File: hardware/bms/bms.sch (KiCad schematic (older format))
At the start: 199 parts, among them J1 Conn_01x08, J10 Conn_01x02, J11 Conn_01x02, J12 Conn_01x02, J13 Conn_01x10, J14 Conn_01x02, J15 Conn_01x02, J16 Cell Bypass, J2 Conn_01x04, J3 USB_B_Micro, J4 Conn_01x05, J5 Conn_01x04, J6 Conn_01x04, J7 Conn_01x03, J8 Conn_01x03, J9 Conn_01x02, M1 MountingHole, M2 MountingHole, M3 MountingHole, M4 MountingHole, M5 MountingHole, M6 MountingHole, Q1 BC817, Q10 ZXMP4A16G, Q11 IRF540N, Q12 IRF540N, Q13 BSS138, Q14 IRF540N, Q15 BSS138, Q16 BSS138, Q2 ZXMP4A16G, Q3 BSS138, Q4 BS170, Q5 IRF9540N, Q6 BC847, Q7 IRF9540N, Q8 BSS138, Q9 ZXMP4A16G, SW1 SW_DIP_x03, U1 USBLC6-2SC6, U2 STM32F042C6Tx, U3 TPS560430x3F, U4 TCAN334, U5 MAX485E, U6 LM5164DDAR, U7 LSI94202, Y1 8MHz

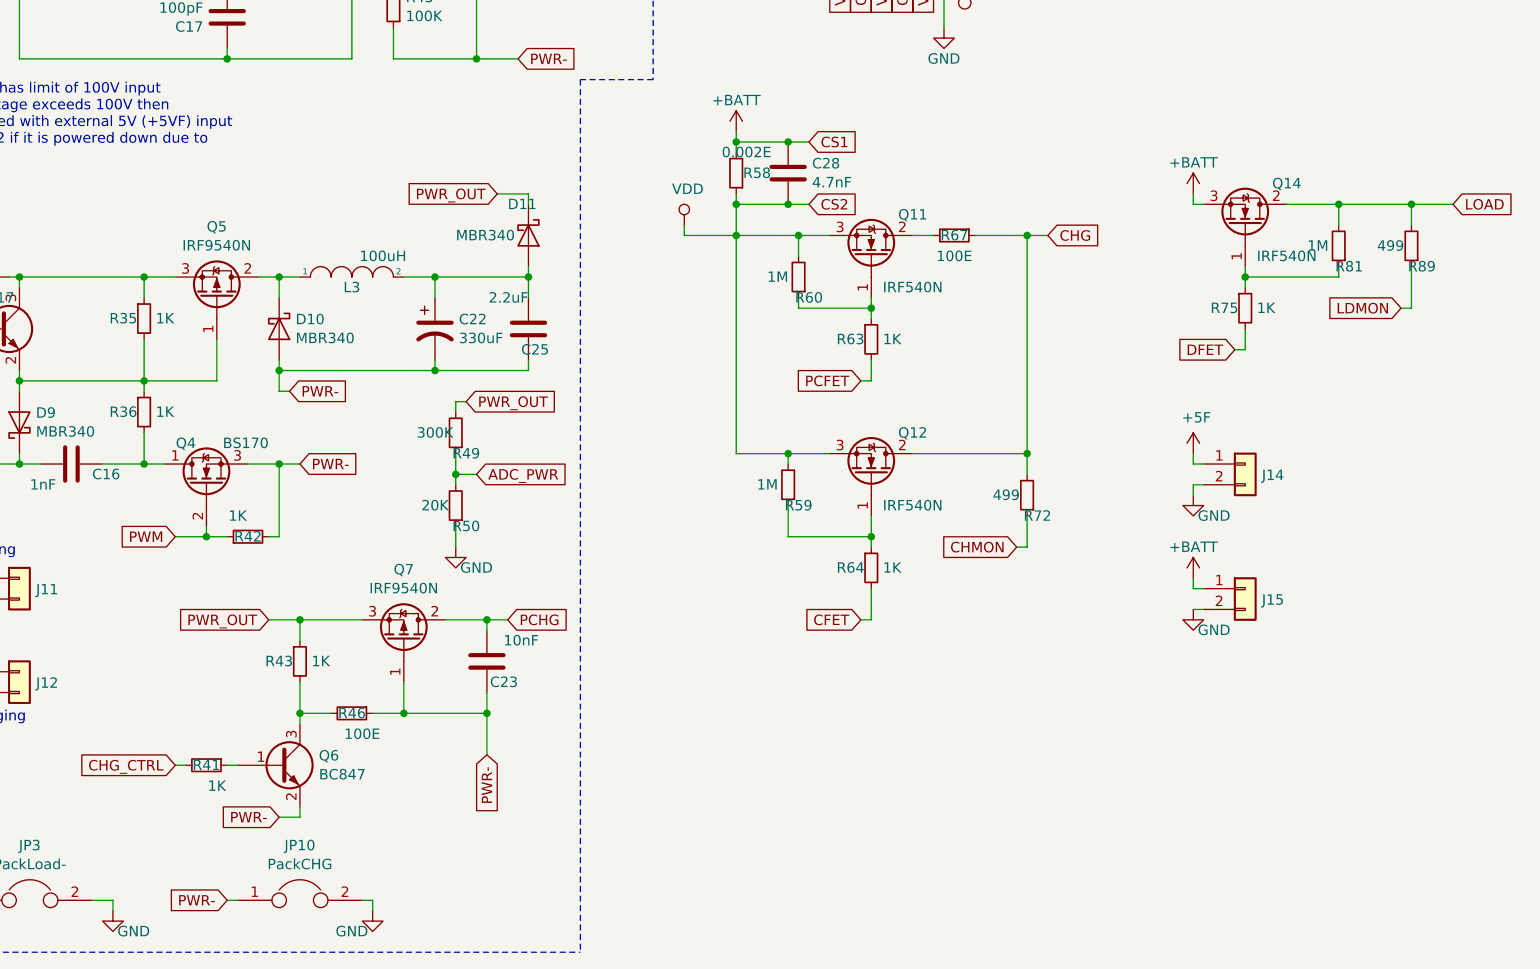
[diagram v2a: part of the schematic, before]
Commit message: fixed schematic errors, added isl94202 ref manual
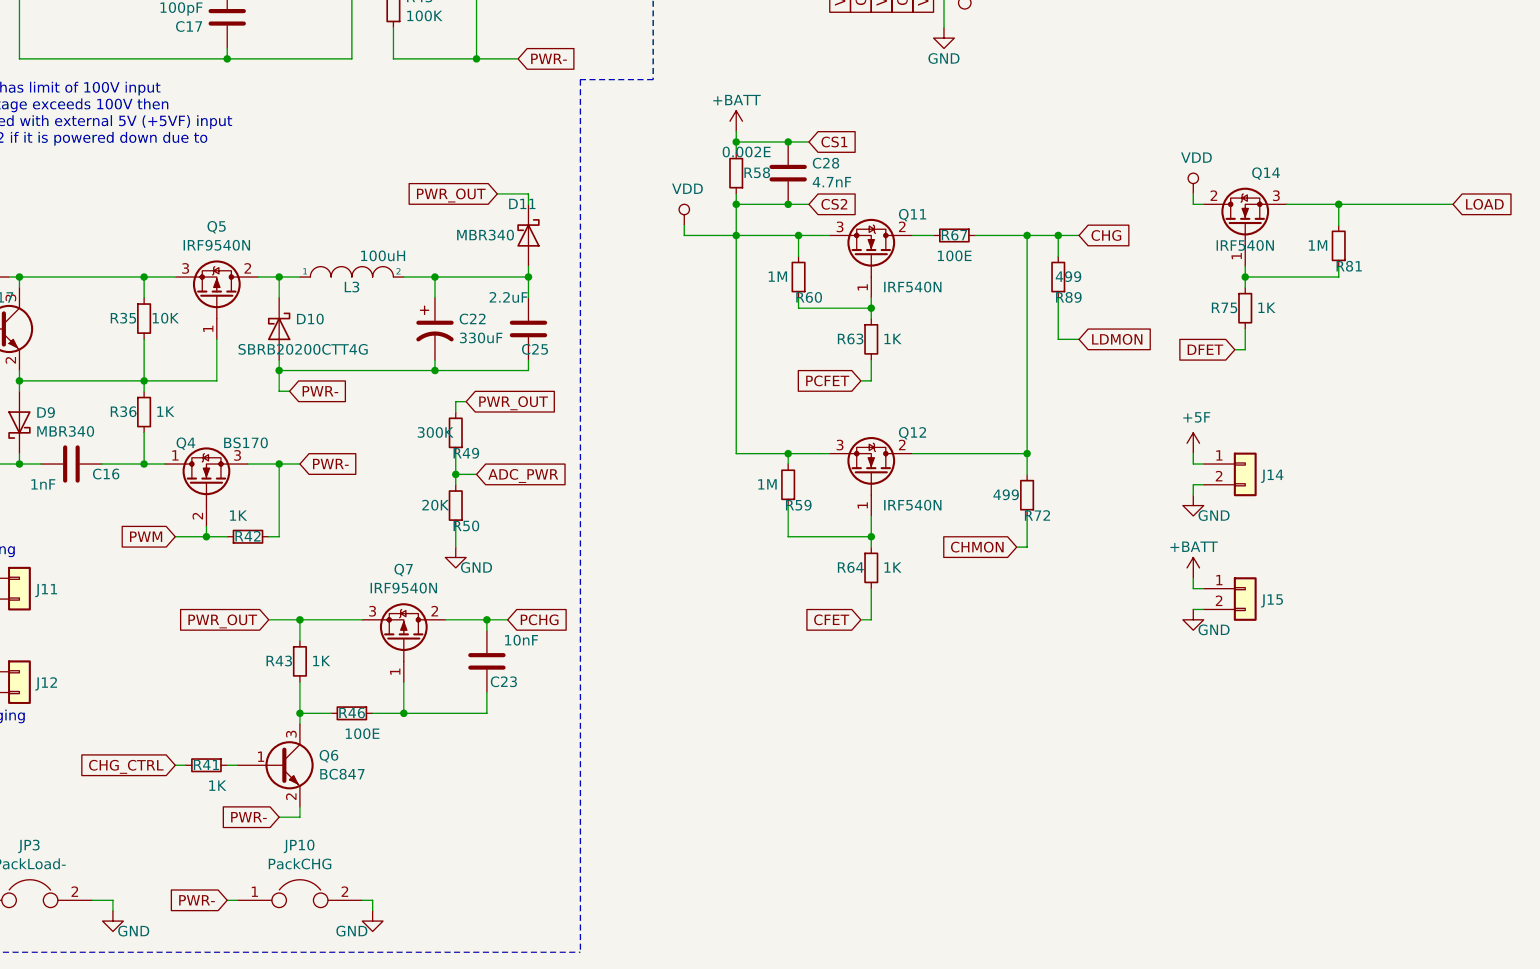
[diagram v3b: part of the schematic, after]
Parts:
- D10: value MBR340 -> SBRB20200CTT4G; footprint Diode_THT:D_DO-201AD_P15.24mm_Horizontal -> bms:D2PAK
- R35: value 1K -> 10K
- U1: footprint Package_SO:TSOP-6_1.65x3.05mm_P0.95mm -> Package_TO_SOT_SMD:SuperSOT-6
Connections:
- net +BATT: no longer Q14.3 (S)
- net CHG: now also R89.2
- net LOAD: now also Q14.3 (S); no longer Q14.2 (D), R89.2
- net PWR-: no longer C23.1, Q7.1 (G), R46.1
- net VDD: now also Q14.2 (D)
- new net: C23.1, Q7.1 (G), R46.1
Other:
- moved on the sheet: R89
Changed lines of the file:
@@
 F 0 "U1" H 1700 10766 50  0000 C CNN
 F 1 "USBLC6-2SC6" H 1700 10675 50  0000 C CNN
-F 2 "Package_SO:TSOP-6_1.65x3.05mm_P0.95mm" H 1700 9850 50  0001 C CNN
+F 2 "Package_TO_SOT_SMD:SuperSOT-6" H 1700 9850 50  0001 C CNN
 F 3 "" H 1450 10650 50  0001 C CNN
 	1    1700 10300
@@
 	1    0    0    -1
 $EndComp
-Text GLabel 13750 7600 2    50   Input ~ 0
+Text GLabel 13900 7600 2    50   Input ~ 0
 CHG
-Wire Wire Line
-	13400 7600 13650 7600
 Text GLabel 12850 8300 0    50   Input ~ 0
 PCFET
@@
 Connection ~ 13650 7600
 Wire Wire Line
-	13650 7600 13750 7600
+	13650 7600 13800 7600
 Wire Wire Line
 	12500 8700 12500 8650
@@
 Text GLabel 12850 9450 0    50   Input ~ 0
 CFET
-$Comp
-L power:+BATT #PWR0138
-U 1 1 5F6BE9DF
-P 14450 7400
-F 0 "#PWR0138" H 14450 7250 50  0001 C CNN
-F 1 "+BATT" H 14450 7550 50  0000 C CNN
-F 2 "" H 14450 7400 50  0001 C CNN
-F 3 "" H 14450 7400 50  0001 C CNN
-	1    14450 7400
-	1    0    0    -1
-$EndComp
 Wire Wire Line
 	14450 7400 14450 7450
@@
 Text GLabel 15700 7450 2    50   Input ~ 0
 LOAD
-Wire Wire Line
-	15150 7450 15500 7450
 Connection ~ 15150 7450
 $Comp
 L Device:R_Small R89
 U 1 1 5F80EB43
-P 15500 7650
-F 0 "R89" H 15450 7750 50  0000 C CNN
-F 1 "499" H 15600 7650 50  0000 C CNN
-F 2 "Resistor_SMD:R_0603_1608Metric_Pad1.05x0.95mm_HandSolder" H 15500 7650 50  0001 C CNN
-F 3 "~" H 15500 7650 50  0001 C CNN
-	1    15500 7650
+P 13800 7800
+F 0 "R89" H 13750 7900 50  0000 C CNN
+F 1 "499" H 13750 7800 50  0000 C CNN
+F 2 "Resistor_SMD:R_0603_1608Metric_Pad1.05x0.95mm_HandSolder" H 13800 7800 50  0001 C CNN
+F 3 "~" H 13800 7800 50  0001 C CNN
+	1    13800 7800
 	-1   0    0    1
 $EndComp
 Wire Wire Line
-	15500 7550 15500 7450
-Connection ~ 15500 7450
-Wire Wire Line
-	15500 7450 15700 7450
+	13800 7700 13800 7600
 $Comp
 L Device:R_Small R72
@@
 Text GLabel 13600 9100 0    50   Input ~ 0
 CHMON
-Text GLabel 15450 7950 0    50   Input ~ 0
+Text GLabel 13900 8100 2    50   Input ~ 0
 LDMON
 Wire Wire Line
@@
 	14700 8050 14700 8150
 Wire Wire Line
-	15450 7950 15500 7950
-Wire Wire Line
-	15500 7750 15500 7950
+	13800 7900 13800 8100
 $Comp
 L power:VDD #PWR0139
@@
 P 10050 8050
 F 0 "D10" V 10004 8129 50  0000 L CNN
-F 1 "MBR340" V 10095 8129 50  0000 L CNN
-F 2 "Diode_THT:D_DO-201AD_P15.24mm_Horizontal" H 10050 7875 50  0001 C CNN
+F 1 "SBRB20200CTT4G" V 10150 7850 50  0000 L CNN
+F 2 "bms:D2PAK" H 10050 7875 50  0001 C CNN
 F 3 "http://www.onsemi.com/pub_link/Collateral/MBR340-D.PDF" H 10050 8050 50  0001 C CNN
 	1    10050 8050
@@
 P 9400 8000
 F 0 "R35" H 9300 8000 50  0000 C CNN
-F 1 "1K" H 9500 8000 50  0000 C CNN
+F 1 "10K" H 9500 8000 50  0000 C CNN
 F 2 "Resistor_SMD:R_0603_1608Metric_Pad1.05x0.95mm_HandSolder" H 9400 8000 50  0001 C CNN
 F 3 "~" H 9400 8000 50  0001 C CNN
@@
 Wire Wire Line
 	10050 10400 10150 10400
-Text GLabel 11050 10100 3    50   Input ~ 0
-PWR-
-Wire Wire Line
-	11050 9900 11050 10100
-Connection ~ 11050 9900
 Text GLabel 9800 10800 0    50   Input ~ 0
 PWR-
@@
 	6950 9400 7050 9400
 $Comp
-L Transistor_FET:IRF540N Q11
-U 1 1 60664D6A
-P 12900 7700
-F 0 "Q11" V 13100 7900 50  0000 C CNN
-F 1 "IRF540N" V 12750 7900 50  0000 C CNN
-F 2 "Package_TO_SOT_SMD:TO-263-2" H 13150 7625 50  0001 L CIN
-F 3 "http://www.irf.com/product-info/datasheets/data/irf540n.pdf" H 12900 7700 50  0001 L CNN
-	1    12900 7700
-	0    1    -1   0
-$EndComp
-$Comp
 L Transistor_FET:IRF540N Q12
 U 1 1 606EC197
@@
 U 1 1 606EDC47
 P 14700 7550
-F 0 "Q14" V 14900 7750 50  0000 C CNN
-F 1 "IRF540N" V 14550 7750 50  0000 C CNN
+F 0 "Q14" V 14950 7450 50  0000 C CNN
+F 1 "IRF540N" V 14600 7550 50  0000 C CNN
 F 2 "Package_TO_SOT_SMD:TO-263-2" H 14950 7475 50  0001 L CIN
 F 3 "http://www.irf.com/product-info/datasheets/data/irf540n.pdf" H 14700 7550 50  0001 L CNN
 	1    14700 7550
-	0    1    -1   0
+	0    -1   -1   0
 $EndComp
 $Comp
@@
 Wire Notes Line
 	11500 6850 11500 11050
+$Comp
+L Transistor_FET:IRF540N Q11
+U 1 1 60664D6A
+P 12900 7700
+F 0 "Q11" V 13100 7900 50  0000 C CNN
+F 1 "IRF540N" V 12750 7900 50  0000 C CNN
+F 2 "Package_TO_SOT_SMD:TO-263-2" H 13150 7625 50  0001 L CIN
+F 3 "http://www.irf.com/product-info/datasheets/data/irf540n.pdf" H 12900 7700 50  0001 L CNN
+	1    12900 7700
+	0    1    -1   0
+$EndComp
+$Comp
+L power:VDD #PWR?
+U 1 1 60A78516
+P 14450 7400
+F 0 "#PWR?" H 14450 7250 50  0001 C CNN
+F 1 "VDD" H 14467 7573 50  0000 C CNN
+F 2 "" H 14450 7400 50  0001 C CNN
+F 3 "" H 14450 7400 50  0001 C CNN
+	1    14450 7400
+	1    0    0    -1
+$EndComp
+Wire Wire Line
+	15150 7450 15700 7450
+Connection ~ 13800 7600
+Wire Wire Line
+	13800 7600 13900 7600
+Wire Wire Line
+	13400 7600 13650 7600
+Wire Wire Line
+	13800 8100 13900 8100
 $EndSCHEMATC

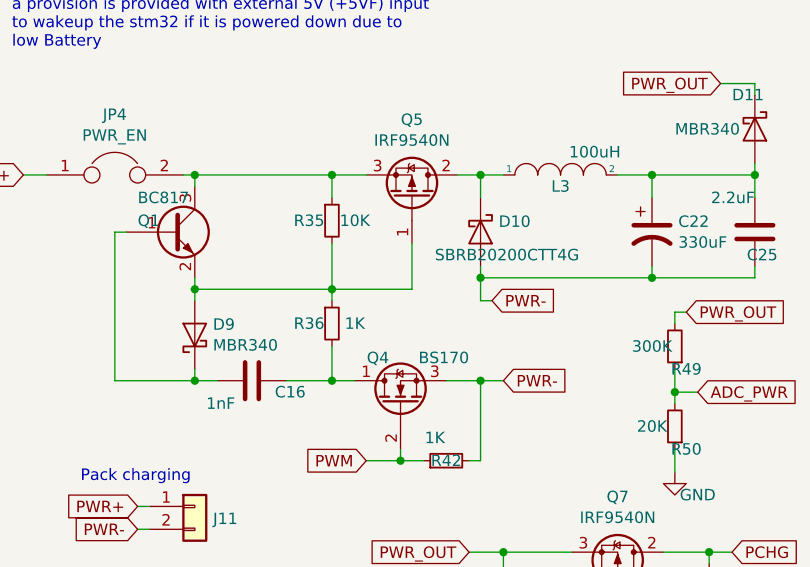
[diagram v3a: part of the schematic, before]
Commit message: footprint corrections
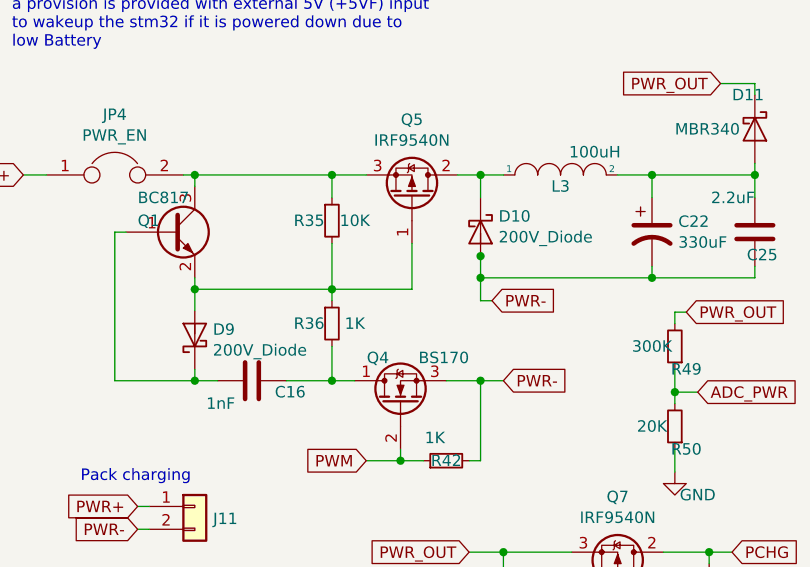
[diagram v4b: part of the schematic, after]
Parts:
- removed D10: SBRB20200CTT4G, bms:D2PAK, symbol Diode:MBR340
- removed D9: MBR340, Diode_THT:D_DO-201AD_P15.24mm_Horizontal, symbol Diode:MBR340
- added D10, D9: 200V_Diode, bms:D2PAK, symbol BMS:200V_Diode
- R2, R3, R33, R34, R37, R38, R39, R40, R51, R52, R54, R55, R56, R57, R65, R66, R68, R69, R70, R71, R78, R80, R83, R84, R85, R86, R87: footprint Resistor_SMD:R_1210_3225Metric_Pad1.42x2.65mm_HandSolder -> Resistor_SMD:R_0603_1608Metric_Pad1.05x0.95mm_HandSolder
- U4: footprint Package_SO:SOIC-8-N7_3.9x4.9mm_P1.27mm -> Package_SO:SOIC-8_3.9x4.9mm_P1.27mm
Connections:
- net PWR-: now also D10.1, D10.3
- net at Q1.2 (E), Q5.1 (G), R35.2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: now also D9.1, D9.3
- net at L3.1, Q5.2 (D): now also D10.4
- net at C16.2, Q1.1 (B): now also D9.4

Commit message: Added i2c level shifter
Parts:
- removed C25: 2.2uF, Capacitor_SMD:C_0603_1608Metric_Pad1.05x0.95mm_HandSolder, symbol Device:C
- removed D11: MBR340, Diode_THT:D_DO-201AD_P15.24mm_Horizontal, symbol Diode:MBR340
- added C25: 10uF, Capacitor_Tantalum_SMD:CP_EIA-7132-28_AVX-C, symbol Device:CP1
- added D11: 200V_Diode, bms:D2PAK, symbol BMS:200V_Diode
- added R90, R91: 4K7, Resistor_SMD:R_0603_1608Metric_Pad1.05x0.95mm_HandSolder, symbol Device:R_Small
- added R92: 200K, Resistor_SMD:R_0603_1608Metric_Pad1.05x0.95mm_HandSolder, symbol Device:R_Small
- added U8: PCA9306, Package_SO:SSOP-8_2.95x2.8mm_P0.65mm, symbol Interface:PCA9306
- C22: value 330uF -> 10uF; footprint Capacitor_Tantalum_SMD:CP_EIA-3528-21_Kemet-B -> Capacitor_Tantalum_SMD:CP_EIA-7132-28_AVX-C
- C23: value 10nF -> 0.01uF; footprint Capacitor_SMD:C_0603_1608Metric_Pad1.05x0.95mm_HandSolder -> Capacitor_SMD:C_1206_3216Metric_Pad1.42x1.75mm_HandSolder
- R49, R50: footprint Resistor_SMD:R_0603_1608Metric_Pad1.05x0.95mm_HandSolder -> Resistor_SMD:R_1206_3216Metric_Pad1.42x1.75mm_HandSolder
- R6, R9: value 2K2 -> 4K7
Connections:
- net CHG: no longer R89.2
- net GND: now also U7.49 (EP), U8.1 (GND)
- net LOAD: now also R89.2
- net PWR-: now also C25.2
- net PWR_OUT: now also D11.4
- net SCL: now also R91.1, U8.3 (SCL1); no longer R9.1, U2.42 (PB6)
- net SDA: now also R90.1, U8.4 (SDA1); no longer R6.1, U2.43 (PB7)
- net VCC: now also R92.1
- net RGO: now reaches TP5.1, U7.36 (RGO)
- net RGO: now also R90.2, R91.2, U8.2 (VREF1)
- net at C22.1, L3.2: now also C25.1, D11.1, D11.3
- new net: R92.2, U8.7 (VREF2), U8.8 (EN)
- new net SCL_3.3: R9.1, U2.42 (PB6), U8.6 (SCL2)
- new net SDA_3.3: R6.1, U2.43 (PB7), U8.5 (SDA2)
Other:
- moved on the sheet: D10, R6, R89, R9, TP5

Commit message: Schematics and footprint corrections
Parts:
- added FB2: Ferrite_Bead_Small, Inductor_SMD:L_0805_2012Metric_Pad1.15x1.40mm_HandSolder, symbol Device:Ferrite_Bead_Small
- added NT1: Net-Tie_2, NetTie:NetTie-2_THT_Pad1.0mm, symbol Device:Net-Tie_2
- Q10, Q2, Q9: value ZXMP4A16G -> NX3008PBK; footprint Package_TO_SOT_SMD:SOT-223-3_TabPin2 -> Package_TO_SOT_SMD:SOT-23
- Q4: footprint Package_TO_SOT_THT:TO-92_Inline -> Package_TO_SOT_SMD:SOT-23W_Handsoldering
- Q5, Q7: footprint Package_TO_SOT_THT:TO-220-3_Vertical -> Package_TO_SOT_SMD:TO-263-2
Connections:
- net GND: now also FB2.1, NT1.2; no longer C10.2, C18.2, C19.2, C26.2, C27.2, C31.2, C32.2, C33.2, C34.2, JP10.2, JP3.2, R50.1, R88.2, U7.18 (VSS), U7.28 (VSS), U7.29 (VSS), U7.49 (EP)
- net GNDA: now also C18.2, C19.2, C26.2, C27.2, C31.2, C32.2, C33.2, C34.2, JP10.2, JP3.2, R50.1, R88.2, U7.18 (VSS), U7.28 (VSS), U7.29 (VSS), U7.49 (EP), NT1.1; no longer U2.8 (VSSA)
- net RGO: now also R76.1, R77.1, R79.1, R82.1
- net VCC: no longer R76.1, R77.1, R79.1, R82.1
- new net GNDS: C10.2, FB2.2, U2.8 (VSSA)
